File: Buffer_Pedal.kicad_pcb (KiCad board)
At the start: 2 copper layers, 20.9 x 21.2 mm, 17 parts, among them Q1 J113, Q2 J113

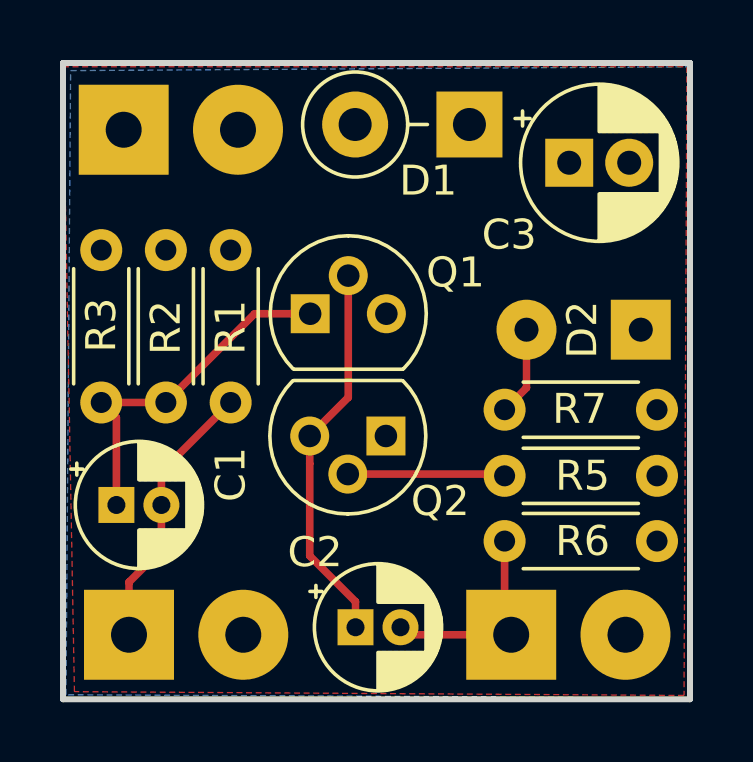
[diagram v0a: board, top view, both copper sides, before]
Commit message: fixed JFET pinout
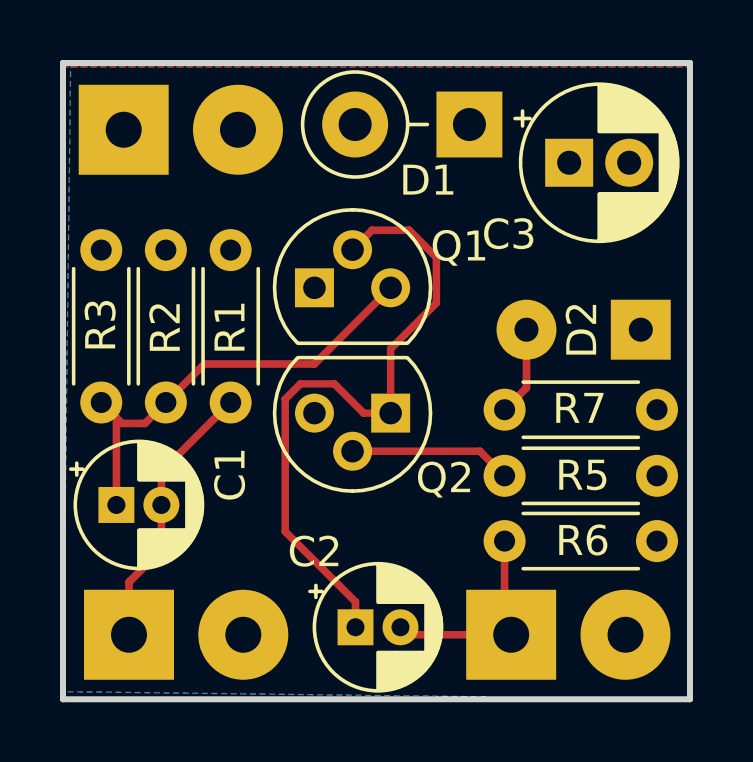
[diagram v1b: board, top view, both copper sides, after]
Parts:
- moved G*** 10.5 mm to (61.7, 110.5)
- moved Q1 0.88 mm to (61.7, 103.1)
- moved Q2 0.78 mm to (64.3, 107.3)
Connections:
- Q1 pad 1: Net-(C1-Pad1) -> PWR
- Q1 pad 3: PWR -> Net-(C1-Pad1)
- Q2 pad 1: GND -> Net-(C2-Pad1)
- Q2 pad 3: Net-(C2-Pad1) -> GND
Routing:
- net Net-(C2-Pad1): track 12.9 -> 22.0 mm
- net Net-(C1-Pad1): track 11.8 -> 15.4 mm
- net Net-(Q2-Pad2): track 5.25 -> 5.90 mm
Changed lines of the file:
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@@
     (thickness 1.6)
     (drawings 4)
-    (tracks 28)
+    (tracks 39)
     (zones 0)
     (modules 17)
@@
   (page A4)
   (layers
-    (0 F.Cu signal hide)
-    (31 B.Cu signal hide)
+    (0 F.Cu signal)
+    (31 B.Cu signal)
     (32 B.Adhes user)
     (33 F.Adhes user)
@@
     (45 Margin user)
     (46 B.CrtYd user hide)
-    (47 F.CrtYd user hide)
+    (47 F.CrtYd user)
     (48 B.Fab user hide)
     (49 F.Fab user hide)
   )
   (setup
-    (last_trace_width 0.254)
+    (last_trace_width 0.25)
     (user_trace_width 0.254)
     (trace_clearance 0.2)
@@
   )
   (module tst:Bluet (layer B.Cu)
-    (at 66.548 101.219 180)
+    (at 61.722 110.49 180)
     (fp_text reference G*** (at 0 0 180) (layer B.SilkS) hide
       (effects (font (size 1.524 1.524) (thickness 0.3)) (justify mirror))
@@
   )
   (module Package_TO_SOT_THT:TO-92 (layer F.Cu)
-    (at 64.104 108.064 180)
+    (at 64.262 107.302 180)
     (descr "TO-92 leads molded, narrow, drill 0.75mm (see NXP sot054_po.pdf)")
     (tags "to-92 sc-43 sc-43a sot54 PA33 transistor")
@@
     (fp_line (start -0.53 1.85) (end 3.07 1.85) (layer F.SilkS) (width 0.12))
     (pad 1 thru_hole rect (at 0 0 270) (size 1.3 1.3) (drill 0.75) (layers *.Cu *.Mask)
+      (net 4 "Net-(C2-Pad1)"))
+    (pad 3 thru_hole circle (at 2.54 0 270) (size 1.3 1.3) (drill 0.75) (layers *.Cu *.Mask)
       (net 5 GND))
-    (pad 3 thru_hole circle (at 2.54 0 270) (size 1.3 1.3) (drill 0.75) (layers *.Cu *.Mask)
-      (net 4 "Net-(C2-Pad1)"))
     (pad 2 thru_hole circle (at 1.27 -1.27 270) (size 1.3 1.3) (drill 0.75) (layers *.Cu *.Mask)
       (net 8 "Net-(Q2-Pad2)"))
@@
   )
   (module Package_TO_SOT_THT:TO-92 (layer F.Cu)
-    (at 61.579 103.989)
+    (at 61.722 103.124)
     (descr "TO-92 leads molded, narrow, drill 0.75mm (see NXP sot054_po.pdf)")
     (tags "to-92 sc-43 sc-43a sot54 PA33 transistor")
@@
     (fp_line (start -0.53 1.85) (end 3.07 1.85) (layer F.SilkS) (width 0.12))
     (pad 1 thru_hole rect (at 0 0 90) (size 1.3 1.3) (drill 0.75) (layers *.Cu *.Mask)
+      (net 6 PWR))
+    (pad 3 thru_hole circle (at 2.54 0 90) (size 1.3 1.3) (drill 0.75) (layers *.Cu *.Mask)
       (net 2 "Net-(C1-Pad1)"))
-    (pad 3 thru_hole circle (at 2.54 0 90) (size 1.3 1.3) (drill 0.75) (layers *.Cu *.Mask)
-      (net 6 PWR))
     (pad 2 thru_hole circle (at 1.27 -1.27 90) (size 1.3 1.3) (drill 0.75) (layers *.Cu *.Mask)
       (net 4 "Net-(C2-Pad1)"))
@@
   (segment (start 55.119801 107.451801) (end 54.615 106.947) (width 0.254) (layer F.Cu) (net 2))
   (segment (start 55.119801 110.363) (end 55.119801 107.451801) (width 0.254) (layer F.Cu) (net 2))
-  (segment (start 54.615 106.947) (end 56.769 106.947) (width 0.254) (layer F.Cu) (net 2))
-  (segment (start 59.727 103.989) (end 61.579 103.989) (width 0.254) (layer F.Cu) (net 2))
-  (segment (start 56.769 106.947) (end 59.727 103.989) (width 0.254) (layer F.Cu) (net 2))
+  (segment (start 64.262 103.124) (end 61.722 105.664) (width 0.25) (layer F.Cu) (net 2))
+  (segment (start 58.052 105.664) (end 56.769 106.947) (width 0.25) (layer F.Cu) (net 2))
+  (segment (start 61.722 105.664) (end 58.052 105.664) (width 0.25) (layer F.Cu) (net 2))
+  (segment (start 55.314999 107.646999) (end 54.615 106.947) (width 0.25) (layer F.Cu) (net 2))
+  (segment (start 56.069001 107.646999) (end 55.314999 107.646999) (width 0.25) (layer F.Cu) (net 2))
+  (segment (start 56.769 106.947) (end 56.069001 107.646999) (width 0.25) (layer F.Cu) (net 2))
   (segment (start 68.03 114.44) (end 68.28 114.69) (width 0.25) (layer F.Cu) (net 3) (status 30))
   (segment (start 68.28 111.68) (end 68.04 111.44) (width 0.25) (layer F.Cu) (net 3) (status 30))
@@
   (segment (start 64.84 114.69) (end 64.59 114.44) (width 0.254) (layer F.Cu) (net 3))
   (segment (start 68.28 114.69) (end 64.84 114.69) (width 0.254) (layer F.Cu) (net 3))
-  (segment (start 62.849 106.779) (end 61.564 108.064) (width 0.254) (layer F.Cu) (net 4))
-  (segment (start 62.849 102.719) (end 62.849 106.779) (width 0.254) (layer F.Cu) (net 4))
-  (segment (start 61.564 108.983238) (end 61.564 108.064) (width 0.254) (layer F.Cu) (net 4))
-  (segment (start 61.564 112.06) (end 61.564 108.983238) (width 0.254) (layer F.Cu) (net 4))
-  (segment (start 63.09 113.586) (end 61.564 112.06) (width 0.254) (layer F.Cu) (net 4))
-  (segment (start 63.09 114.44) (end 63.09 113.586) (width 0.254) (layer F.Cu) (net 4))
+  (segment (start 63.641999 101.204001) (end 64.882001 101.204001) (width 0.25) (layer F.Cu) (net 4))
+  (segment (start 62.992 101.854) (end 63.641999 101.204001) (width 0.25) (layer F.Cu) (net 4))
+  (segment (start 64.882001 101.204001) (end 65.786 102.108) (width 0.25) (layer F.Cu) (net 4))
+  (segment (start 65.786 102.108) (end 65.786 103.632) (width 0.25) (layer F.Cu) (net 4))
+  (segment (start 64.262 105.156) (end 64.262 107.302) (width 0.25) (layer F.Cu) (net 4))
+  (segment (start 65.786 103.632) (end 64.262 105.156) (width 0.25) (layer F.Cu) (net 4))
+  (segment (start 63.09 113.59) (end 63.09 114.44) (width 0.25) (layer F.Cu) (net 4))
+  (segment (start 60.746999 111.246999) (end 63.09 113.59) (width 0.25) (layer F.Cu) (net 4))
+  (segment (start 60.746999 106.833999) (end 60.746999 111.246999) (width 0.25) (layer F.Cu) (net 4))
+  (segment (start 61.253999 106.326999) (end 60.746999 106.833999) (width 0.25) (layer F.Cu) (net 4))
+  (segment (start 63.362 107.302) (end 62.386999 106.326999) (width 0.25) (layer F.Cu) (net 4))
+  (segment (start 62.386999 106.326999) (end 61.253999 106.326999) (width 0.25) (layer F.Cu) (net 4))
+  (segment (start 64.262 107.302) (end 63.362 107.302) (width 0.25) (layer F.Cu) (net 4))
   (segment (start 68.79 106.458) (end 68.79 104.521) (width 0.254) (layer F.Cu) (net 7))
   (segment (start 68.06 107.188) (end 68.79 106.458) (width 0.254) (layer F.Cu) (net 7))
   (segment (start 68.002 109.334) (end 68.06 109.392) (width 0.254) (layer F.Cu) (net 8))
-  (segment (start 62.834 109.334) (end 68.002 109.334) (width 0.254) (layer F.Cu) (net 8))
+  (segment (start 67.24 108.572) (end 68.06 109.392) (width 0.25) (layer F.Cu) (net 8))
+  (segment (start 62.58 108.572) (end 67.24 108.572) (width 0.25) (layer F.Cu) (net 8))
   (zone (net 5) (net_name GND) (layer B.Cu) (hatch edge 0.508)
     (connect_pads (clearance 0.508))
     (min_thickness 0.254)
-    (fill yes (arc_segments 32) (thermal_gap 0.508) (thermal_bridge_width 0.508) (smoothing fillet))
+    (fill yes (arc_segments 32) (thermal_gap 0.508) (thermal_bridge_width 0.508))
     (polygon
       (pts
-        (xy 53.594 95.885) (xy 74.14 95.758) (xy 74.19 116.79) (xy 53.44 116.69)
+        (xy 53.594 95.758) (xy 74.168 95.758) (xy 74.168 116.84) (xy 53.34 116.586)
       )
     )
@@
     (connect_pads (clearance 0.508))
     (min_thickness 0.254)
-    (fill yes (arc_segments 32) (thermal_gap 0.508) (thermal_bridge_width 0.508) (smoothing fillet))
+    (fill yes (arc_segments 32) (thermal_gap 0.508) (thermal_bridge_width 0.508))
     (polygon
       (pts
-        (xy 53.337479 95.758) (xy 74.137479 95.758) (xy 74.041 116.713) (xy 53.721 116.586)
+        (xy 53.34 95.758) (xy 74.168 95.758) (xy 74.168 116.84) (xy 53.34 116.84)
       )
     )

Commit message: updated schematic and layout
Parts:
- moved Q1 3.84 mm to (65.5, 102.6), turned to 180 degrees
- moved Q2 1.56 mm to (63.0, 108.2), turned to 0 degrees
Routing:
- net Net-(C2-Pad1): track 22.0 -> 11.1 mm
- net Net-(C1-Pad1): track 15.4 -> 14.4 mm
- net Net-(Q2-Pad2): track 5.90 -> 4.96 mm
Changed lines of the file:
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@@
     (thickness 1.6)
     (drawings 4)
-    (tracks 39)
+    (tracks 31)
     (zones 0)
     (modules 17)
@@
   )
   (module Package_TO_SOT_THT:TO-92 (layer F.Cu)
-    (at 64.262 107.302 180)
+    (at 62.992 108.204)
     (descr "TO-92 leads molded, narrow, drill 0.75mm (see NXP sot054_po.pdf)")
     (tags "to-92 sc-43 sc-43a sot54 PA33 transistor")
-    (fp_text reference Q2 (at -1.809 -2.172 180) (layer F.SilkS)
+    (fp_text reference Q2 (at -1.809 -2.172) (layer F.SilkS)
+      (effects (font (size 1 1) (thickness 0.15)))
+    )
+    (fp_text value J113 (at 1.27 2.79) (layer F.Fab)
+      (effects (font (size 1 1) (thickness 0.15)))
+    )
+    (fp_arc (start 1.27 0) (end 1.27 -2.6) (angle 135) (layer F.SilkS) (width 0.12))
+    (fp_arc (start 1.27 0) (end 1.27 -2.48) (angle -135) (layer F.Fab) (width 0.1))
+    (fp_arc (start 1.27 0) (end 1.27 -2.6) (angle -135) (layer F.SilkS) (width 0.12))
+    (fp_arc (start 1.27 0) (end 1.27 -2.48) (angle 135) (layer F.Fab) (width 0.1))
+    (fp_line (start 4 2.01) (end -1.46 2.01) (layer F.CrtYd) (width 0.05))
+    (fp_line (start 4 2.01) (end 4 -2.73) (layer F.CrtYd) (width 0.05))
+    (fp_line (start -1.46 -2.73) (end -1.46 2.01) (layer F.CrtYd) (width 0.05))
+    (fp_line (start -1.46 -2.73) (end 4 -2.73) (layer F.CrtYd) (width 0.05))
+    (fp_line (start -0.5 1.75) (end 3 1.75) (layer F.Fab) (width 0.1))
+    (fp_line (start -0.53 1.85) (end 3.07 1.85) (layer F.SilkS) (width 0.12))
+    (pad 1 thru_hole rect (at 0 0 90) (size 1.3 1.3) (drill 0.75) (layers *.Cu *.Mask)
+      (net 4 "Net-(C2-Pad1)"))
+    (pad 3 thru_hole circle (at 2.54 0 90) (size 1.3 1.3) (drill 0.75) (layers *.Cu *.Mask)
+      (net 5 GND))
+    (pad 2 thru_hole circle (at 1.27 -1.27 90) (size 1.3 1.3) (drill 0.75) (layers *.Cu *.Mask)
+      (net 8 "Net-(Q2-Pad2)"))
+    (model ${KISYS3DMOD}/Package_TO_SOT_THT.3dshapes/TO-92.wrl
+      (at (xyz 0 0 0))
+      (scale (xyz 1 1 1))
+      (rotate (xyz 0 0 0))
+    )
+  )
+  (module Package_TO_SOT_THT:TO-92 (layer F.Cu)
+    (at 65.532 102.616 180)
+    (descr "TO-92 leads molded, narrow, drill 0.75mm (see NXP sot054_po.pdf)")
+    (tags "to-92 sc-43 sc-43a sot54 PA33 transistor")
+    (fp_text reference Q1 (at 4.318 -2.032 180) (layer F.SilkS)
       (effects (font (size 1 1) (thickness 0.15)))
     )
@@
     (fp_line (start -0.53 1.85) (end 3.07 1.85) (layer F.SilkS) (width 0.12))
     (pad 1 thru_hole rect (at 0 0 270) (size 1.3 1.3) (drill 0.75) (layers *.Cu *.Mask)
-      (net 4 "Net-(C2-Pad1)"))
+      (net 6 PWR))
     (pad 3 thru_hole circle (at 2.54 0 270) (size 1.3 1.3) (drill 0.75) (layers *.Cu *.Mask)
-      (net 5 GND))
+      (net 2 "Net-(C1-Pad1)"))
     (pad 2 thru_hole circle (at 1.27 -1.27 270) (size 1.3 1.3) (drill 0.75) (layers *.Cu *.Mask)
-      (net 8 "Net-(Q2-Pad2)"))
-    (model ${KISYS3DMOD}/Package_TO_SOT_THT.3dshapes/TO-92.wrl
-      (at (xyz 0 0 0))
-      (scale (xyz 1 1 1))
-      (rotate (xyz 0 0 0))
-    )
-  )
-  (module Package_TO_SOT_THT:TO-92 (layer F.Cu)
-    (at 61.722 103.124)
-    (descr "TO-92 leads molded, narrow, drill 0.75mm (see NXP sot054_po.pdf)")
-    (tags "to-92 sc-43 sc-43a sot54 PA33 transistor")
-    (fp_text reference Q1 (at 4.842 -1.373) (layer F.SilkS)
-      (effects (font (size 1 1) (thickness 0.15)))
-    )
-    (fp_text value J113 (at 1.27 2.79) (layer F.Fab)
-      (effects (font (size 1 1) (thickness 0.15)))
-    )
-    (fp_arc (start 1.27 0) (end 1.27 -2.6) (angle 135) (layer F.SilkS) (width 0.12))
-    (fp_arc (start 1.27 0) (end 1.27 -2.48) (angle -135) (layer F.Fab) (width 0.1))
-    (fp_arc (start 1.27 0) (end 1.27 -2.6) (angle -135) (layer F.SilkS) (width 0.12))
-    (fp_arc (start 1.27 0) (end 1.27 -2.48) (angle 135) (layer F.Fab) (width 0.1))
-    (fp_line (start 4 2.01) (end -1.46 2.01) (layer F.CrtYd) (width 0.05))
-    (fp_line (start 4 2.01) (end 4 -2.73) (layer F.CrtYd) (width 0.05))
-    (fp_line (start -1.46 -2.73) (end -1.46 2.01) (layer F.CrtYd) (width 0.05))
-    (fp_line (start -1.46 -2.73) (end 4 -2.73) (layer F.CrtYd) (width 0.05))
-    (fp_line (start -0.5 1.75) (end 3 1.75) (layer F.Fab) (width 0.1))
-    (fp_line (start -0.53 1.85) (end 3.07 1.85) (layer F.SilkS) (width 0.12))
-    (pad 1 thru_hole rect (at 0 0 90) (size 1.3 1.3) (drill 0.75) (layers *.Cu *.Mask)
-      (net 6 PWR))
-    (pad 3 thru_hole circle (at 2.54 0 90) (size 1.3 1.3) (drill 0.75) (layers *.Cu *.Mask)
-      (net 2 "Net-(C1-Pad1)"))
-    (pad 2 thru_hole circle (at 1.27 -1.27 90) (size 1.3 1.3) (drill 0.75) (layers *.Cu *.Mask)
       (net 4 "Net-(C2-Pad1)"))
     (model ${KISYS3DMOD}/Package_TO_SOT_THT.3dshapes/TO-92.wrl
@@
   (segment (start 55.119801 107.451801) (end 54.615 106.947) (width 0.254) (layer F.Cu) (net 2))
   (segment (start 55.119801 110.363) (end 55.119801 107.451801) (width 0.254) (layer F.Cu) (net 2))
-  (segment (start 64.262 103.124) (end 61.722 105.664) (width 0.25) (layer F.Cu) (net 2))
-  (segment (start 58.052 105.664) (end 56.769 106.947) (width 0.25) (layer F.Cu) (net 2))
-  (segment (start 61.722 105.664) (end 58.052 105.664) (width 0.25) (layer F.Cu) (net 2))
   (segment (start 55.314999 107.646999) (end 54.615 106.947) (width 0.25) (layer F.Cu) (net 2))
   (segment (start 56.069001 107.646999) (end 55.314999 107.646999) (width 0.25) (layer F.Cu) (net 2))
   (segment (start 56.769 106.947) (end 56.069001 107.646999) (width 0.25) (layer F.Cu) (net 2))
+  (segment (start 61.1 102.616) (end 56.769 106.947) (width 0.25) (layer F.Cu) (net 2))
+  (segment (start 62.992 102.616) (end 61.1 102.616) (width 0.25) (layer F.Cu) (net 2))
   (segment (start 68.03 114.44) (end 68.28 114.69) (width 0.25) (layer F.Cu) (net 3) (status 30))
   (segment (start 68.28 111.68) (end 68.04 111.44) (width 0.25) (layer F.Cu) (net 3) (status 30))
@@
   (segment (start 64.84 114.69) (end 64.59 114.44) (width 0.254) (layer F.Cu) (net 3))
   (segment (start 68.28 114.69) (end 64.84 114.69) (width 0.254) (layer F.Cu) (net 3))
-  (segment (start 63.641999 101.204001) (end 64.882001 101.204001) (width 0.25) (layer F.Cu) (net 4))
-  (segment (start 62.992 101.854) (end 63.641999 101.204001) (width 0.25) (layer F.Cu) (net 4))
-  (segment (start 64.882001 101.204001) (end 65.786 102.108) (width 0.25) (layer F.Cu) (net 4))
-  (segment (start 65.786 102.108) (end 65.786 103.632) (width 0.25) (layer F.Cu) (net 4))
-  (segment (start 64.262 105.156) (end 64.262 107.302) (width 0.25) (layer F.Cu) (net 4))
-  (segment (start 65.786 103.632) (end 64.262 105.156) (width 0.25) (layer F.Cu) (net 4))
-  (segment (start 63.09 113.59) (end 63.09 114.44) (width 0.25) (layer F.Cu) (net 4))
-  (segment (start 60.746999 111.246999) (end 63.09 113.59) (width 0.25) (layer F.Cu) (net 4))
-  (segment (start 60.746999 106.833999) (end 60.746999 111.246999) (width 0.25) (layer F.Cu) (net 4))
-  (segment (start 61.253999 106.326999) (end 60.746999 106.833999) (width 0.25) (layer F.Cu) (net 4))
-  (segment (start 63.362 107.302) (end 62.386999 106.326999) (width 0.25) (layer F.Cu) (net 4))
-  (segment (start 62.386999 106.326999) (end 61.253999 106.326999) (width 0.25) (layer F.Cu) (net 4))
-  (segment (start 64.262 107.302) (end 63.362 107.302) (width 0.25) (layer F.Cu) (net 4))
+  (segment (start 62.992 105.156) (end 62.992 108.204) (width 0.25) (layer F.Cu) (net 4))
+  (segment (start 64.262 103.886) (end 62.992 105.156) (width 0.25) (layer F.Cu) (net 4))
+  (segment (start 62.992 114.342) (end 63.09 114.44) (width 0.25) (layer F.Cu) (net 4))
+  (segment (start 62.992 108.204) (end 62.992 114.342) (width 0.25) (layer F.Cu) (net 4))
   (segment (start 68.79 106.458) (end 68.79 104.521) (width 0.254) (layer F.Cu) (net 7))
   (segment (start 68.06 107.188) (end 68.79 106.458) (width 0.254) (layer F.Cu) (net 7))
   (segment (start 68.002 109.334) (end 68.06 109.392) (width 0.254) (layer F.Cu) (net 8))
-  (segment (start 67.24 108.572) (end 68.06 109.392) (width 0.25) (layer F.Cu) (net 8))
-  (segment (start 62.58 108.572) (end 67.24 108.572) (width 0.25) (layer F.Cu) (net 8))
+  (segment (start 67.360001 108.692001) (end 68.06 109.392) (width 0.25) (layer F.Cu) (net 8))
+  (segment (start 67.360001 108.588999) (end 67.360001 108.692001) (width 0.25) (layer F.Cu) (net 8))
+  (segment (start 65.705002 106.934) (end 67.360001 108.588999) (width 0.25) (layer F.Cu) (net 8))
+  (segment (start 64.262 106.934) (end 65.705002 106.934) (width 0.25) (layer F.Cu) (net 8))
   (zone (net 5) (net_name GND) (layer B.Cu) (hatch edge 0.508)
     (connect_pads (clearance 0.508))
